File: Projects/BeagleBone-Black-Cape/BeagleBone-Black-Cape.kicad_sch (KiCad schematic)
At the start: 11 parts, among them P8 BeagleBone_Black_Header, P9 BeagleBone_Black_Header, SW1 SW_DIP_x02, U1 CAT24C256

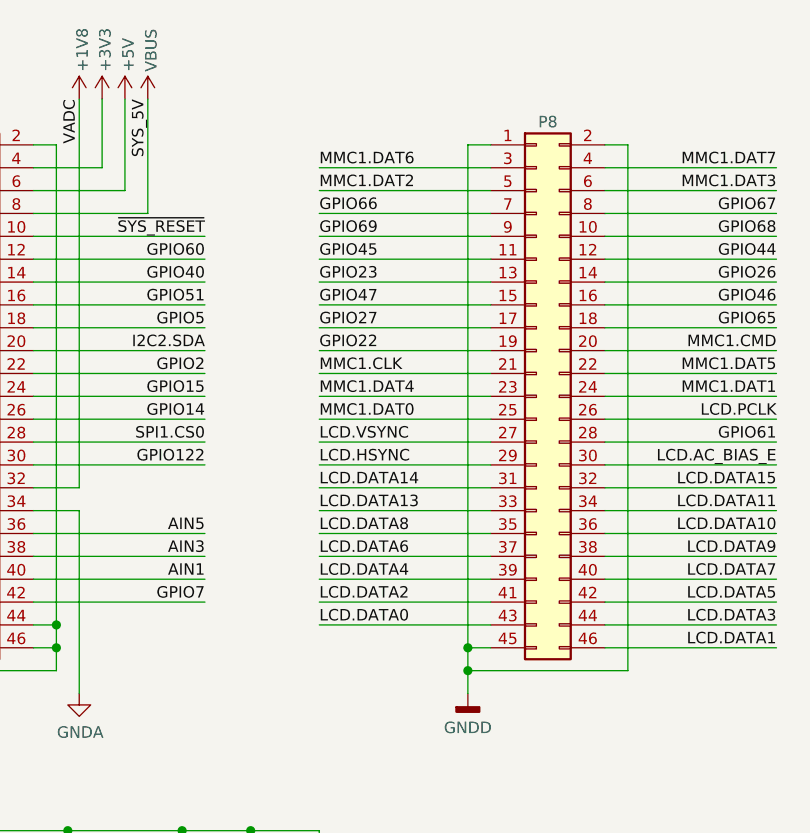
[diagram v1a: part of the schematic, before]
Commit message: Correct BeagleBone Black pinout
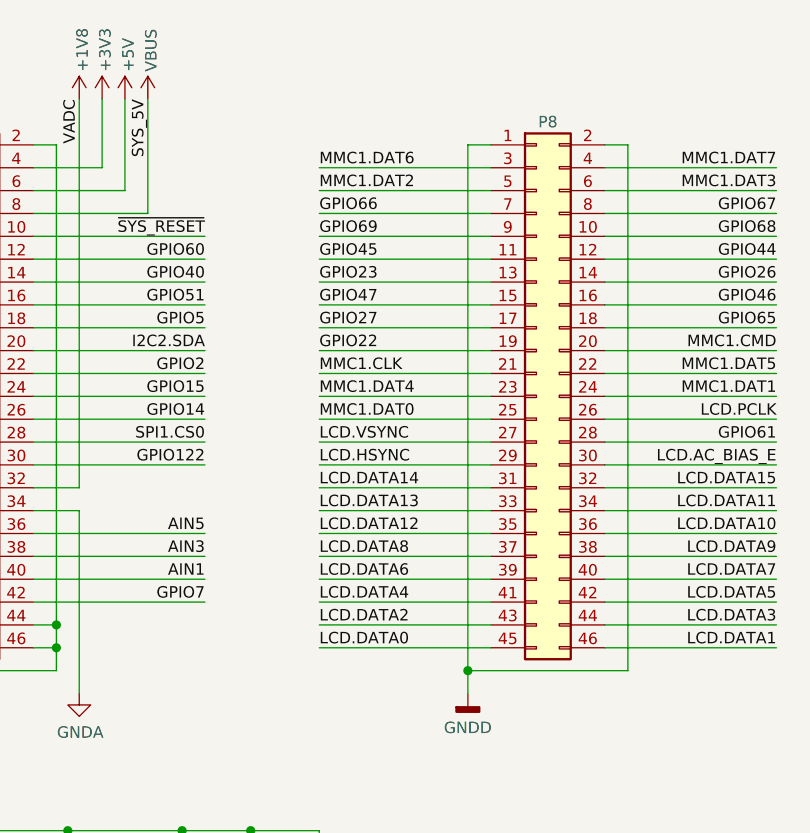
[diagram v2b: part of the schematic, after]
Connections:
- net GNDD: no longer P8.45 (Pin_45)
- net LCD.DATA0: now also P8.45 (Pin_45); no longer P8.43 (Pin_43)
- net LCD.DATA2: now also P8.43 (Pin_43); no longer P8.41 (Pin_41)
- net LCD.DATA4: now also P8.41 (Pin_41); no longer P8.39 (Pin_39)
- net LCD.DATA6: now also P8.39 (Pin_39); no longer P8.37 (Pin_37)
- net LCD.DATA8: now also P8.37 (Pin_37); no longer P8.35 (Pin_35)
- new net LCD.DATA12: P8.35 (Pin_35)
